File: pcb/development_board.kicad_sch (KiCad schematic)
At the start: 29 parts, among them J1 Conn_01x06, J2 TYPE-C-31-M-12, J3 Conn_01x08, J4 Conn_02x09_Top_Bottom, J5 Conn_02x09_Top_Bottom, J6 Conn_02x09_Top_Bottom, J7 Conn_02x09_Top_Bottom, J8 Conn_02x09_Top_Bottom, SW1 SW_DFU, SW2 SW_RST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

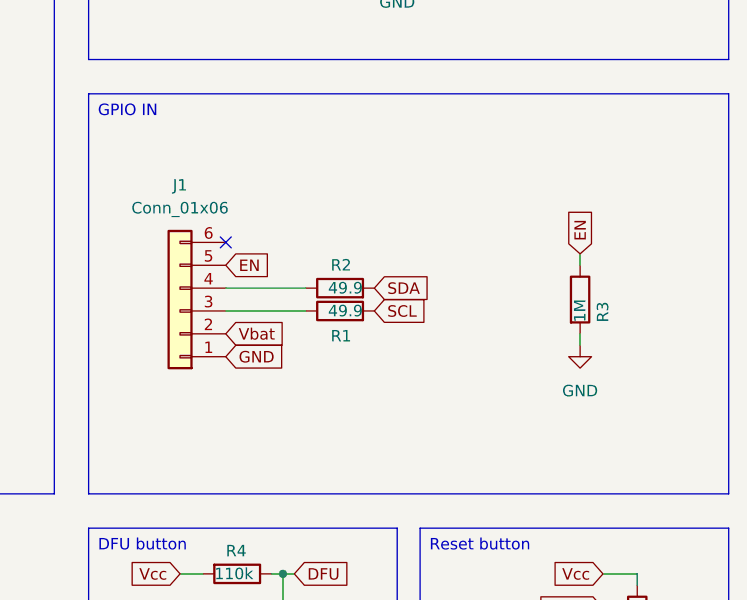
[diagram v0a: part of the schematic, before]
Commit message: fixed enable when running only on usb
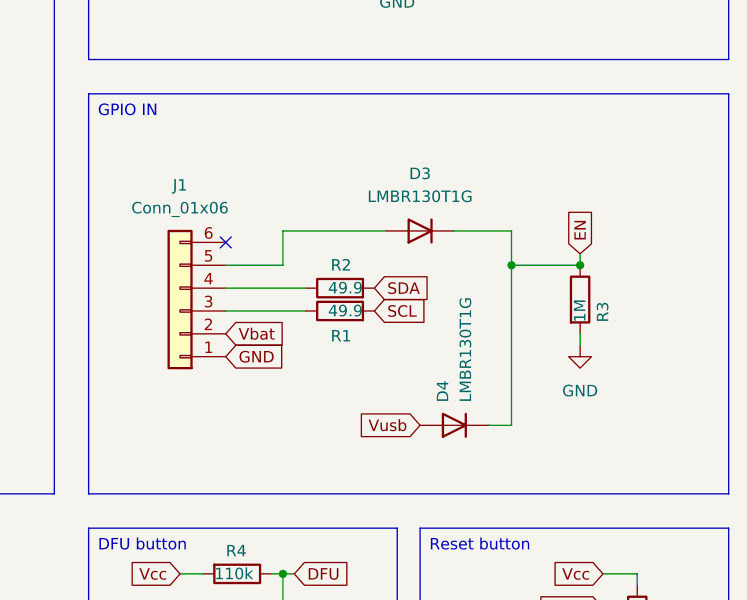
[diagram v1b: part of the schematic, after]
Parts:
- added D3, D4: LMBR130T1G, Diode_SMD:D_SOD-123, symbol Device:D
- J2: Desc (none) -> 5A 1 16P Female Type-C SMD USB Connectors ROHS; JLC (none) -> SMD; LCSC (none) -> C165948
- U2: Desc (none) -> SMD,18x19.2mm WiFi Modules ROHS; JLC (none) -> SMD,18x19.2mm; LCSC (none) -> C3013946; Part (none) -> ESP32-S3-WROOM-1U-N16R8
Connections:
- net EN: now also D3.1 (K), D4.1 (K); no longer J1.5 (Pin_5)
- net Vusb: now also D4.2 (A)
- new net: D3.2 (A), J1.5 (Pin_5)

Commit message: fixed parts selection
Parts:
- SW1, SW2: Desc Without 6mm 100MΩ 300,000 Times 16V 3.3N 5.9mm 5mm Rectangl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 -> None Without 50mA 5.1mm 100000 Times 160gf 12V 5.1mm 1.5mm 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; LCSC C2925580 -> C318884; Part SKPSADE010 -> TS-1187A-B-A-B
- U3: Desc 6V 17V 2 Unidirectional 5.25V SOT-23-6 ESD Protection Devic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 -> 6A 12V 150W 6V Unidirectional 5V SOT-23-6 ESD and Surge Pro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; LCSC C7519 -> C2827654
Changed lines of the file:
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@@
 			)
 		)
-		(property "Desc" "Without 6mm 100MΩ 300,000 Times 16V 3.3N 5.9mm 5mm Rectangle button Brick nogging SPST SMD Tactile Switches ROHS"
+		(property "Desc" "None Without 50mA 5.1mm 100000 Times 160gf 12V 5.1mm 1.5mm Round Button Standing paste SPST SMD Tactile Switches ROHS"
 			(at 259.08 140.97 0)
 			(effects
@@
 			)
 		)
-		(property "LCSC" "C2925580"
+		(property "LCSC" "C318884"
 			(at 259.08 140.97 0)
 			(effects
@@
 			)
 		)
-		(property "Part" "SKPSADE010"
+		(property "Part" "TS-1187A-B-A-B"
 			(at 259.08 140.97 0)
 			(effects
@@
 			)
 		)
-		(property "Desc" "Without 6mm 100MΩ 300,000 Times 16V 3.3N 5.9mm 5mm Rectangle button Brick nogging SPST SMD Tactile Switches ROHS"
+		(property "Desc" "None Without 50mA 5.1mm 100000 Times 160gf 12V 5.1mm 1.5mm Round Button Standing paste SPST SMD Tactile Switches ROHS"
 			(at 222.25 135.89 0)
 			(effects
@@
 			)
 		)
-		(property "LCSC" "C2925580"
+		(property "LCSC" "C318884"
 			(at 222.25 135.89 0)
 			(effects
@@
 			)
 		)
-		(property "Part" "SKPSADE010"
+		(property "Part" "TS-1187A-B-A-B"
 			(at 222.25 135.89 0)
 			(effects
@@
 			)
 		)
-		(property "Desc" "6V 17V 2 Unidirectional 5.25V SOT-23-6 ESD Protection Devices ROHS"
+		(property "Desc" "6A 12V 150W 6V Unidirectional 5V SOT-23-6 ESD and Surge Protection (TVS/ESD) ROHS"
 			(at 167.64 96.52 0)
 			(effects
@@
 			)
 		)
-		(property "LCSC" "C7519"
+		(property "LCSC" "C2827654"
 			(at 167.64 96.52 0)
 			(effects

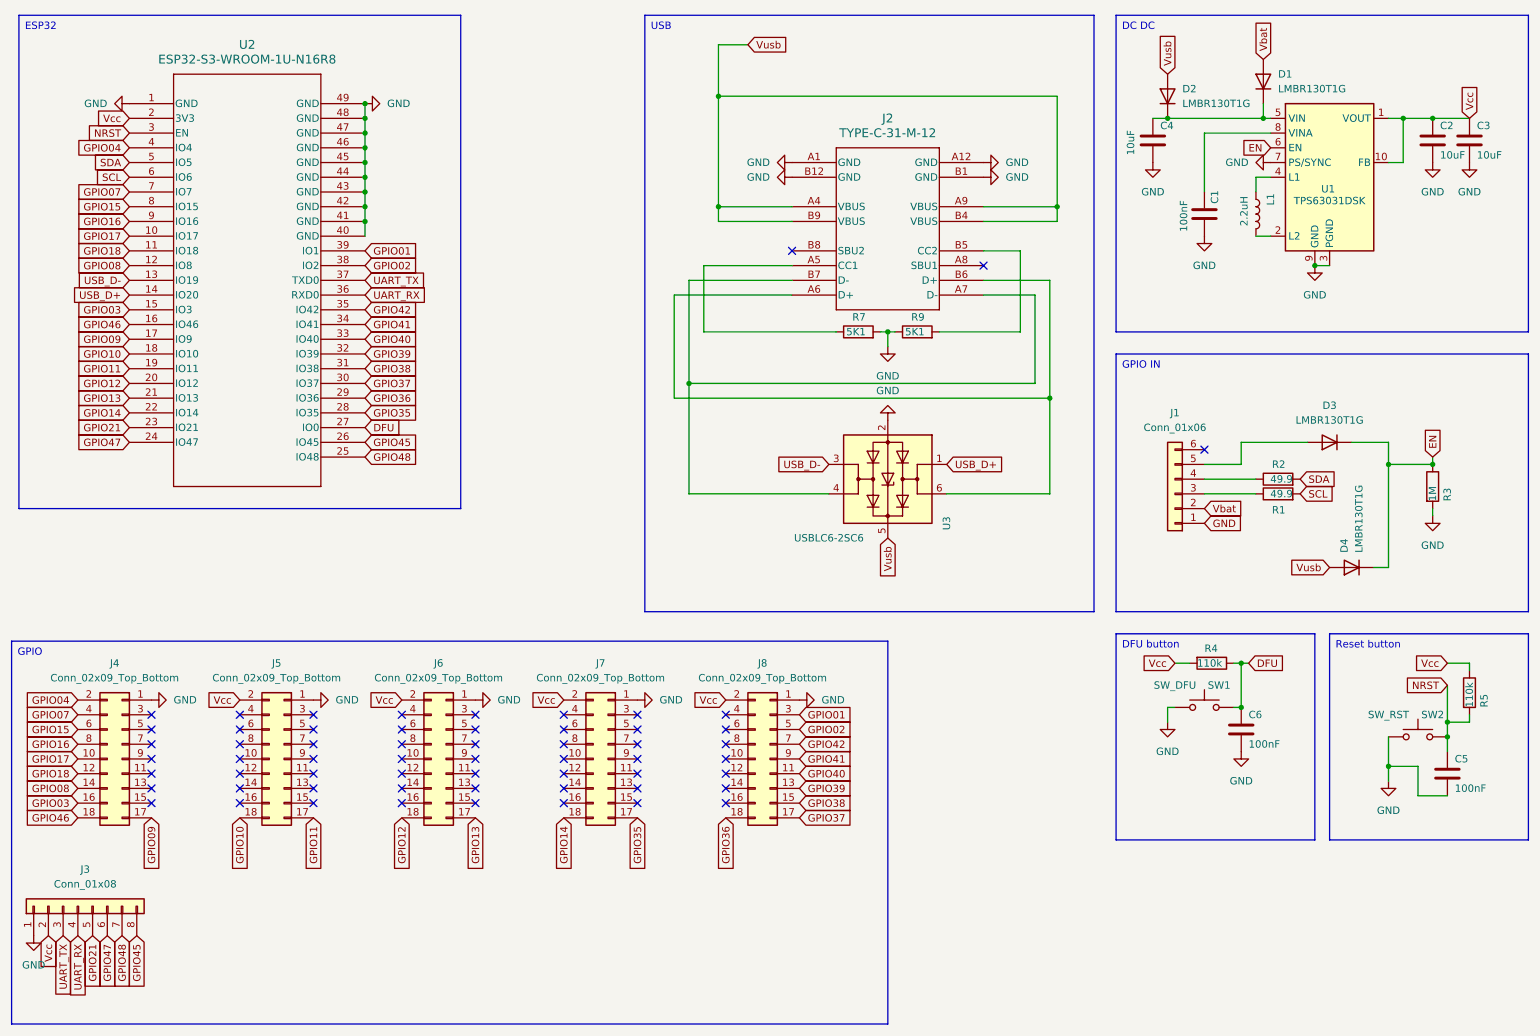
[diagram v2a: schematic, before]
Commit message: added panelized pcb
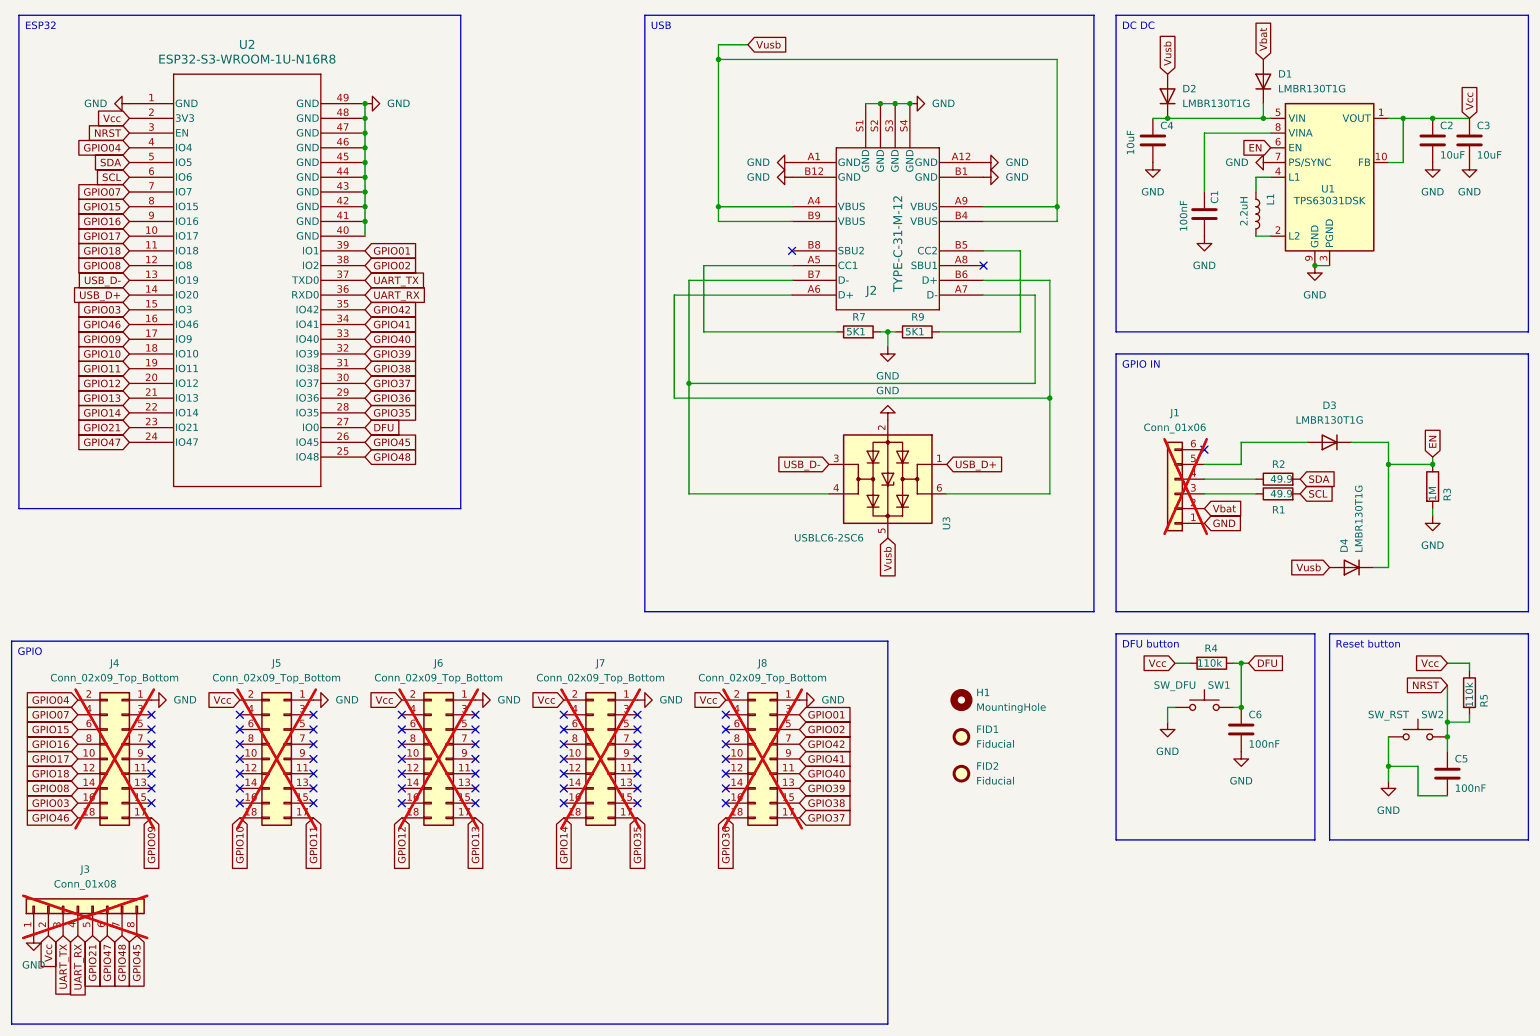
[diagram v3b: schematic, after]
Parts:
- added FID1, FID2: Fiducial, Fiducial:Fiducial_0.75mm_Mask1.5mm, symbol Mechanical:Fiducial
- added H1: MountingHole, MountingHole:MountingHole_2mm, symbol Mechanical:MountingHole
- J1, J3, J4, J5, J6, J7, J8: now not fitted
- J2: footprint Portapack_Mayhem:TYPE-C-31-M-12 -> TYPE-C-31-M-12
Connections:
- net GND: now also J2.S1 (GND), J2.S2 (GND), J2.S3 (GND), J2.S4 (GND)
